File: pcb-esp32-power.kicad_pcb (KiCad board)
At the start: 2 copper layers, 52.6 x 47.4 mm, 52 parts, among them IC1 LTC4091EDJC#PBF, J1 C-OBD-II-16M, J2 Bus_Connector, J3 Conn_01x02, Q1 MMDT5551, Q2 AO3415A, Q3 AO3415A, U1 LTC3530EMS

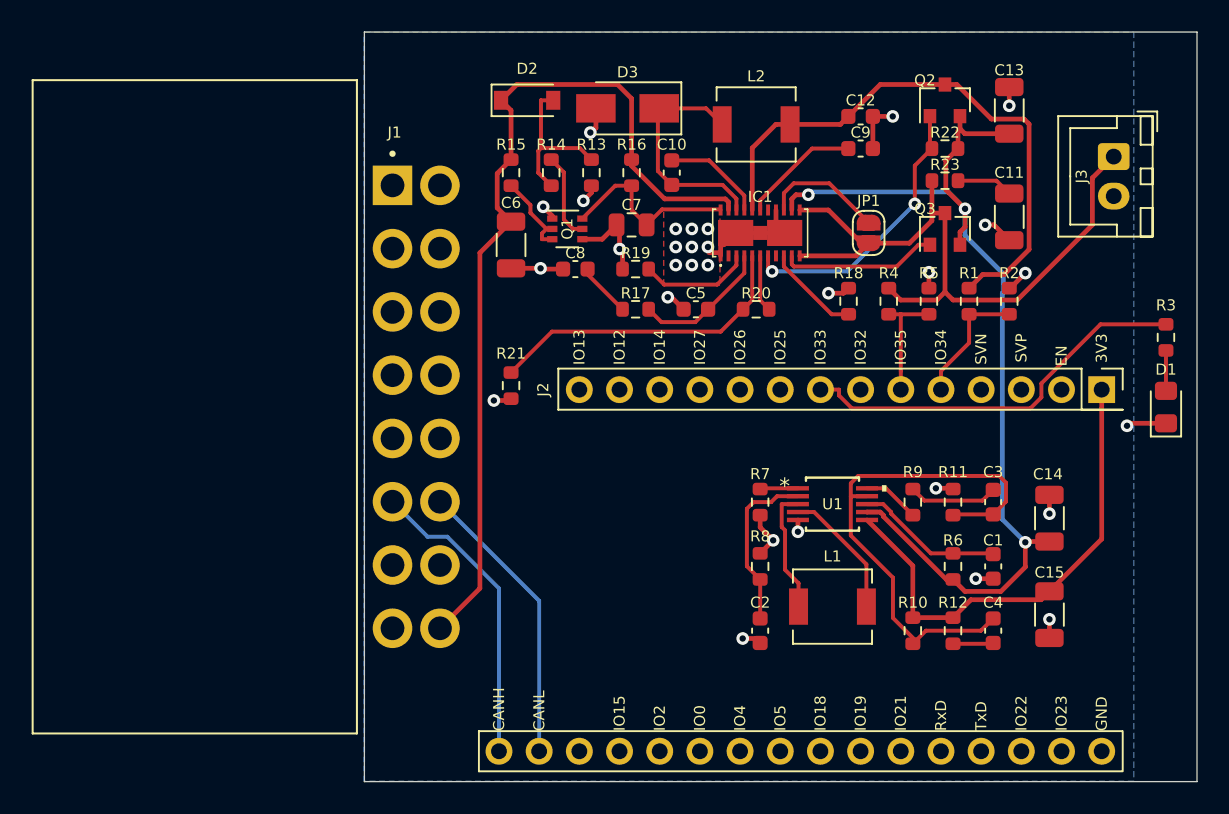
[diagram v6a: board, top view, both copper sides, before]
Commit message: Layout nochmal wg. kritischer Strompfade geändert
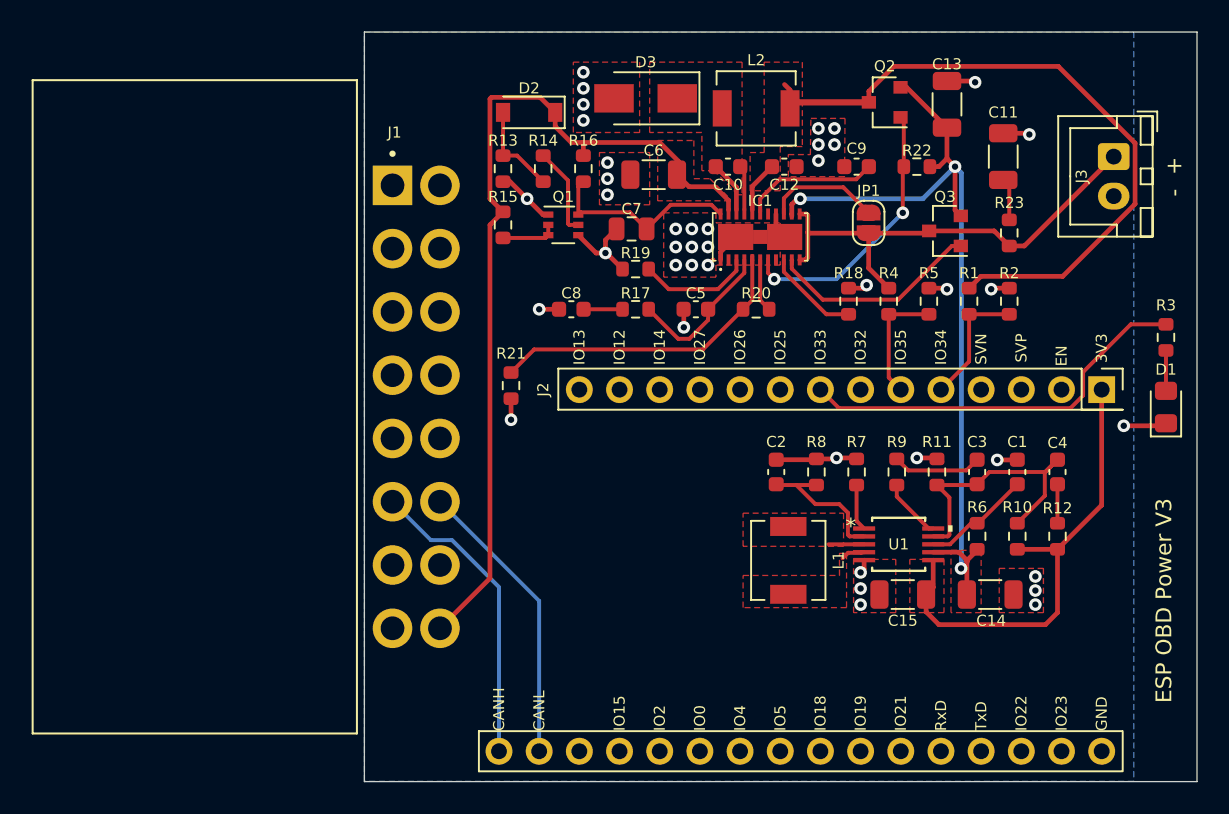
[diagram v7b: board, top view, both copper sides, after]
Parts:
- moved C4 10.8 mm to (170.2, 114.4)
- moved C2 10.1 mm to (152.4, 114.4), turned to 90 degrees
- moved C6 10.1 mm to (144.7, 95.6), turned to 180 degrees
- moved C15 9.36 mm to (160.4, 122.2), turned to 180 degrees
- moved R12 8.90 mm to (170.2, 118.5), turned to 90 degrees
- moved R10 8.90 mm to (167.6, 118.5), turned to 90 degrees
- moved R8 6.95 mm to (154.9, 114.4)
- moved R7 6.39 mm to (157.5, 114.4), turned to 90 degrees
- moved C1 6.16 mm to (167.6, 114.4), turned to 90 degrees
- moved C14 6.11 mm to (165.9, 122.2), turned to 0 degrees
- moved C12 5.78 mm to (152.9, 95.1)
- moved R13 5.59 mm to (135.1, 95.2)
- moved R23 5.24 mm to (167.1, 99.3), turned to 90 degrees
- moved U1 4.90 mm to (160.1, 119.0)
- moved L1 4.04 mm to (153.2, 120.0), turned to 90 degrees
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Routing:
- net Net-(C3-Pad1): track 33.5 -> 17.9 mm
- net +BATT: track 43.3 -> 30.5 mm
- net Net-(C10-Pad1): track 14.8 -> 3.28 mm
- net 5VIN: track 36.9 -> 47.3 mm
- net GND: track 45.1 -> 35.4 mm, vias 30 -> 41
- net 5VOUT: track 63.2 -> 54.6 mm
- net Net-(L1-Pad1): track 8.37 -> 1.53 mm
- net Net-(L1-Pad2): track 7.94 -> 2.26 mm
- net Net-(D2-Pad2): track 10.1 -> 5.95 mm
- net Net-(IC1-Pad10): track 9.90 -> 13.5 mm
- net Net-(C10-Pad2): track 6.42 -> 2.85 mm
- net Net-(C1-Pad1): track 9.34 -> 6.89 mm
- net Net-(Q1-Pad2): track 5.44 -> 3.58 mm
- net Net-(C2-Pad1): track 10.8 -> 9.08 mm
- net Net-(C5-Pad1): track 8.76 -> 10.1 mm
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- added copper zone on F.Cu, net +12V
- added copper zone on F.Cu, net +3V3
- added copper zone on F.Cu, net 5VIN
- added copper zone on F.Cu, net 5VOUT
- added copper zone on F.Cu, net Net-(C10-Pad1)
- added copper zone on F.Cu, net Net-(L1-Pad1)
- added copper zone on F.Cu, net Net-(L1-Pad2)
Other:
- board text added: "- +"
- board text added: "ESP OBD Power V3"
